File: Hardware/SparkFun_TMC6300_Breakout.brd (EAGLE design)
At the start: 15.2 x 20.3 mm, 57 parts, among them U2 TMC6300

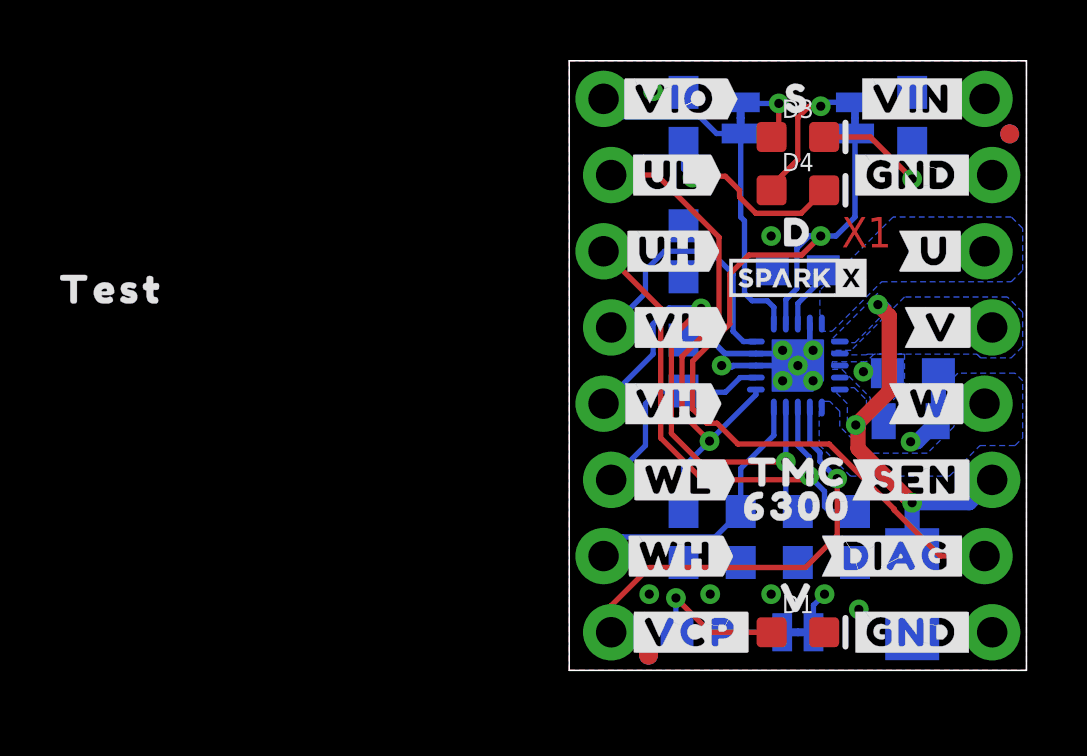
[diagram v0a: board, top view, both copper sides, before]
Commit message: Add readme. Remove old files.
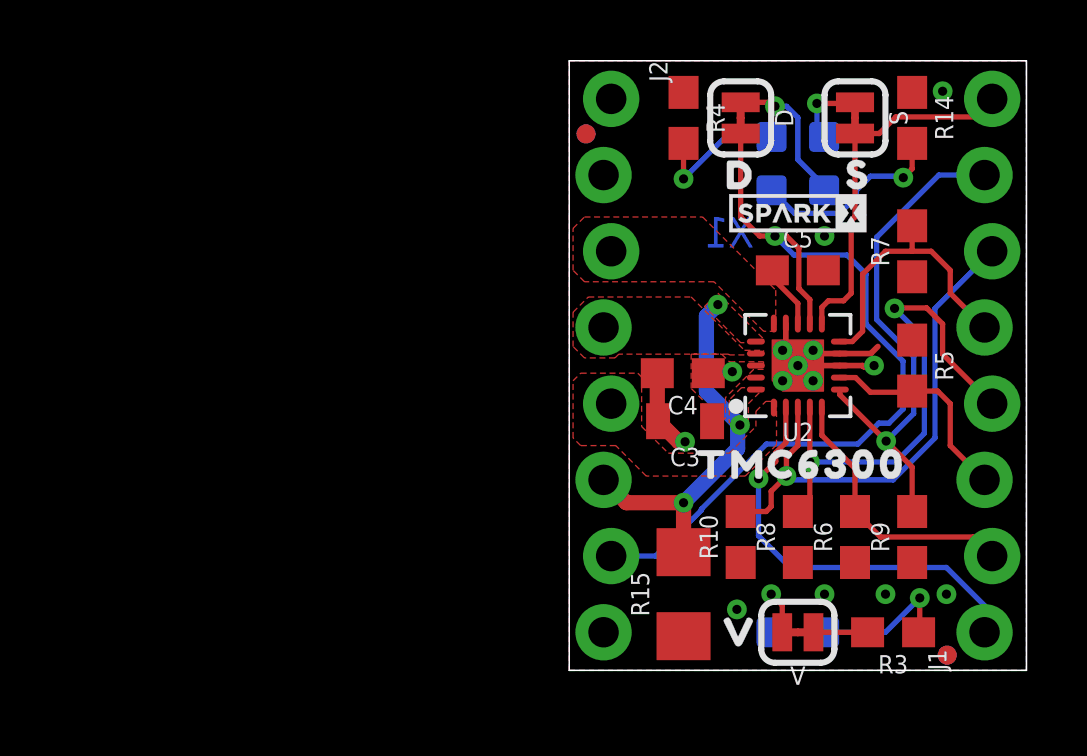
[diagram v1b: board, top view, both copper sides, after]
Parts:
- removed U$4: (no value), output:TEST0
- moved FRAME1 38.1 mm to (-11.4, -11.4), flipped to the top
- moved LOGO2 22.9 mm to (19.1, 50.8), flipped to the top
- moved FD1 14.1 mm to (0.56, 17.9), flipped to the top
- moved FD4 14.1 mm to (0.56, 17.9), flipped to the bottom
- moved J1 12.7 mm to (14.0, 1.27), flipped to the top
- moved J2 12.7 mm to (1.27, 19.1), flipped to the top
- moved LOGO1 10.2 mm to (2.54, -2.54), flipped to the bottom
- moved FD2 9.96 mm to (12.6, 0.51), flipped to the top
- moved FD3 9.96 mm to (12.6, 0.51), flipped to the bottom
- moved U$25 9.65 mm to (2.79, 11.4), flipped to the bottom
- moved U$9 9.14 mm to (3.05, 14.0), flipped to the bottom
- moved U$32 8.89 mm to (3.17, 8.89), flipped to the bottom
- moved U$21 8.64 mm to (11.9, 14.0), flipped to the bottom
- moved U$30 8.64 mm to (11.9, 8.89), flipped to the bottom
- moved U$22 8.38 mm to (11.8, 16.5), flipped to the bottom
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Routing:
- added copper zone on layer 1, net SENSE
- added copper zone on layer 1, net U
- added copper zone on layer 1, net V
- added copper zone on layer 1, net VIN
- added copper zone on layer 1, net W
- removed copper zone on layer 16, net SENSE
- removed copper zone on layer 16, net U
- removed copper zone on layer 16, net V
- removed copper zone on layer 16, net VIN
- removed copper zone on layer 16, net W
